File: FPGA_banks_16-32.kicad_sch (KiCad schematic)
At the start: 2 parts

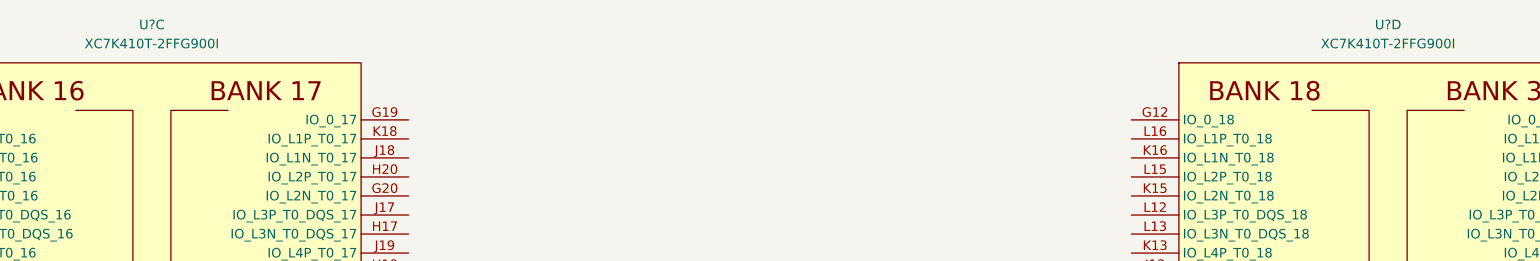
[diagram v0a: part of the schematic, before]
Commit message: Add MT41K512M8DA DDR3L
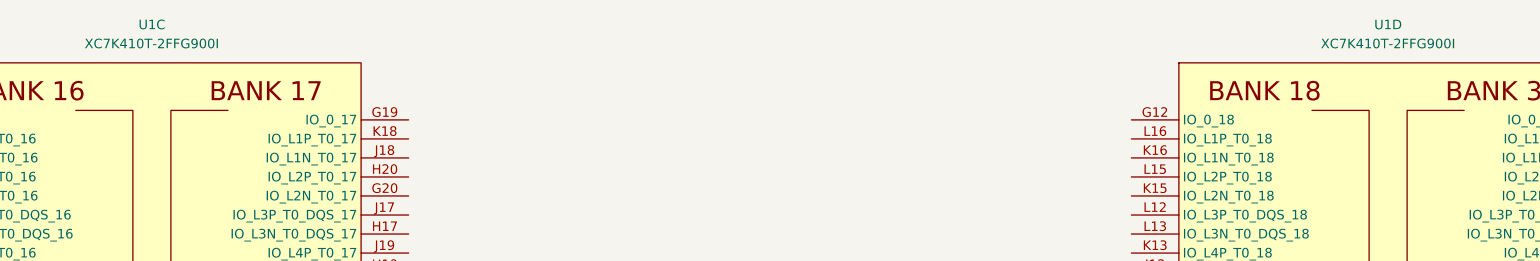
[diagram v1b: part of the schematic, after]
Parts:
- gave numbers to parts that had none: 1
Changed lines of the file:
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@@
   (symbol (lib_id "antmicroMicrocontrollers:XC7K410T-2FFG900I") (at 128.27 137.16 0) (unit 3)
     (in_bom yes) (on_board yes) (fields_autoplaced)
-    (property "Reference" "U?" (id 0) (at 128.27 63.5 0))
+    (property "Reference" "U1" (id 0) (at 128.27 63.5 0))
     (property "Value" "XC7K410T-2FFG900I" (id 1) (at 128.27 66.04 0))
     (property "Footprint" "antmicro-footprints:xc7k410t-2ffg900I" (id 2) (at 128.27 212.09 0)
@@
   (symbol (lib_id "antmicroMicrocontrollers:XC7K410T-2FFG900I") (at 293.37 137.16 0) (unit 4)
     (in_bom yes) (on_board yes) (fields_autoplaced)
-    (property "Reference" "U?" (id 0) (at 293.37 63.5 0))
+    (property "Reference" "U1" (id 0) (at 293.37 63.5 0))
     (property "Value" "XC7K410T-2FFG900I" (id 1) (at 293.37 66.04 0))
     (property "Footprint" "antmicro-footprints:xc7k410t-2ffg900I" (id 2) (at 293.37 212.09 0)

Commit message: Unify title block
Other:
- title: (none) -> K410T devboard
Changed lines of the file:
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@@
   (paper "A3")
   (title_block
-    (comment 1 "www.antmicro.com")
-    (comment 2 "Antmicro Ltd")
+    (title "K410T devboard")
+    (date "2022-12-20")
+    (rev "0.0.99")
   )
   (symbol (lib_id "antmicroMicrocontrollers:XC7K410T-2FFG900I") (at 128.27 137.16 0) (unit 3)
